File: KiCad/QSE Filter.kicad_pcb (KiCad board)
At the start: 2 copper layers, 65.2 x 74.5 mm, 66 parts, among them J1 RF In, J2 RF Out, J3 Power, J4 Control In, Q1 2N7002, Q2 2N7002, Q4 2N7002, Q5 2N7002, U1 EB2-12NU, U2 EB2-12NU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

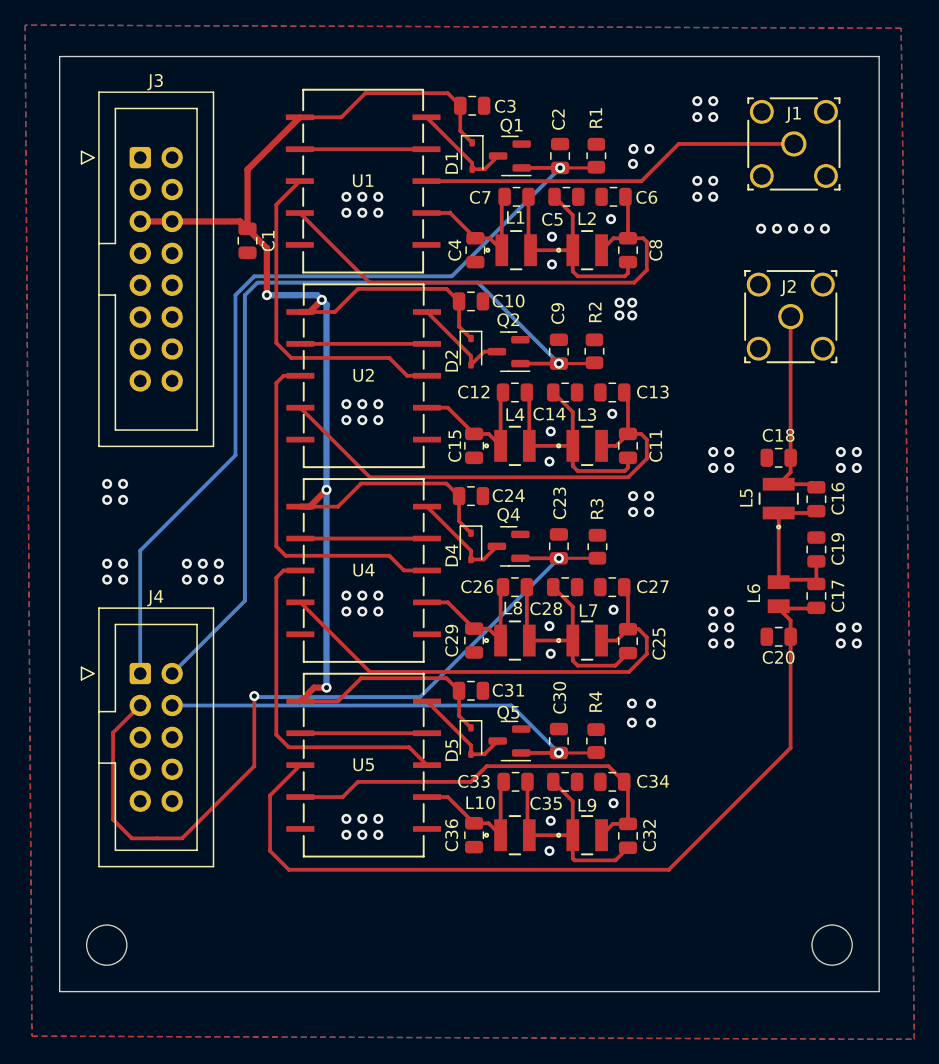
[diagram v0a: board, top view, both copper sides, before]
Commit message: Eliminate acute angles/acid traps in various traces Move C1 slightly
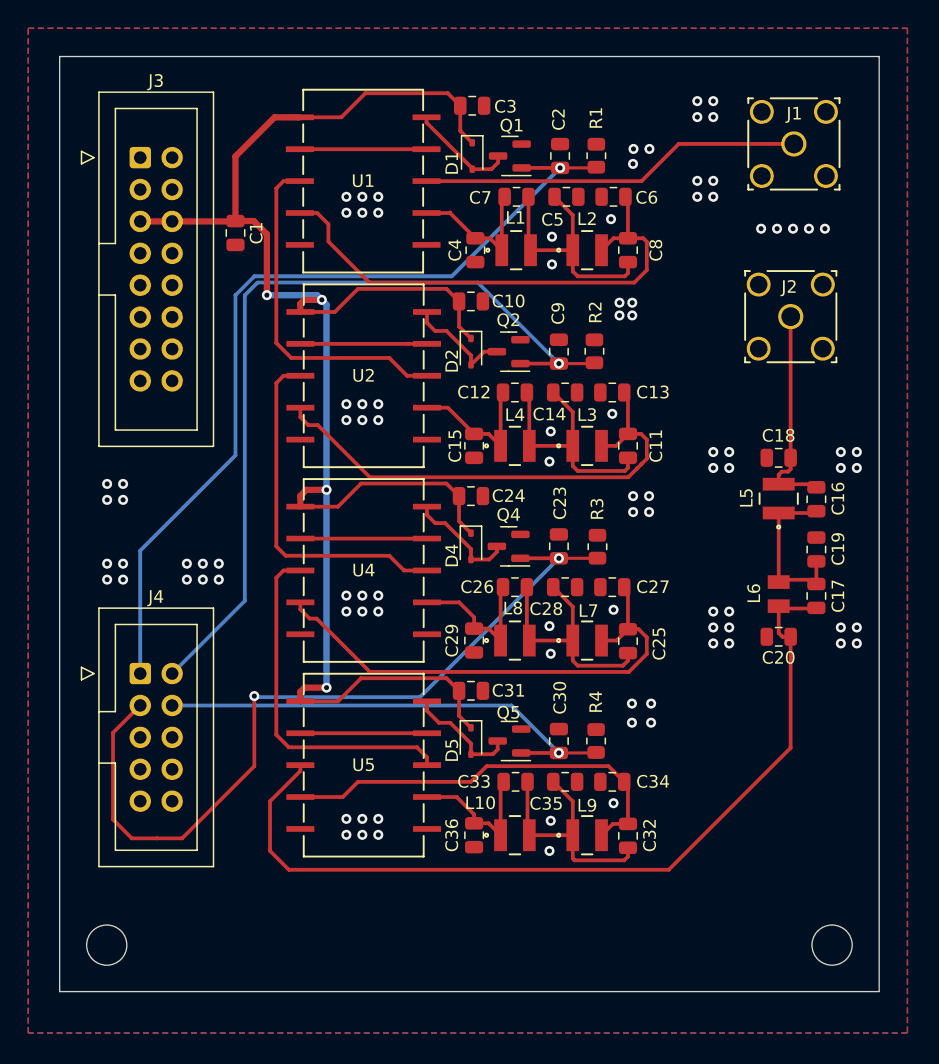
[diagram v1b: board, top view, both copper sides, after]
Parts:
- moved C1 1.14 mm to (91.5, 61.3)
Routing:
- net +12V: track 137.1 -> 140.1 mm
- net Net-(D5-A): track 8.22 -> 9.14 mm
- net Net-(C6-Pad1): track 40.2 -> 41.0 mm
- net 80M_Out: track 26.7 -> 27.5 mm
- net Net-(D4-A): track 8.16 -> 8.88 mm
- net 15M_Out: track 68.4 -> 69.0 mm
- net Net-(D2-A): track 8.16 -> 8.68 mm
- net Net-(C26-Pad1): track 11.4 -> 12.0 mm
